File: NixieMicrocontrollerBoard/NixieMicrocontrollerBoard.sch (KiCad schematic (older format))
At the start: 12 parts, among them IC1 ATMEGA328-P, P1 CONN_01X03, P2 GPS_Header, P3 SD_Header, P4 Nixie_Header, Y1 16MHz

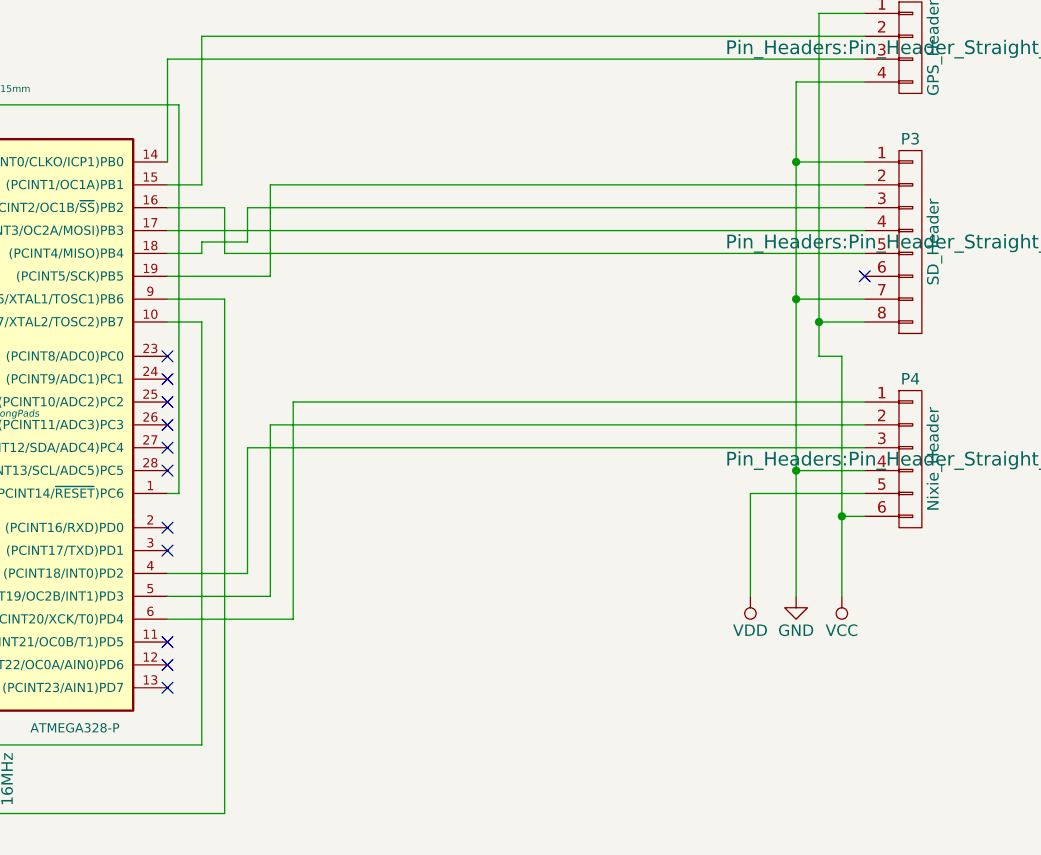
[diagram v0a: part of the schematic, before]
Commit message: Fixes up the microcontroller board, and adds a library to drive the Nixie boards
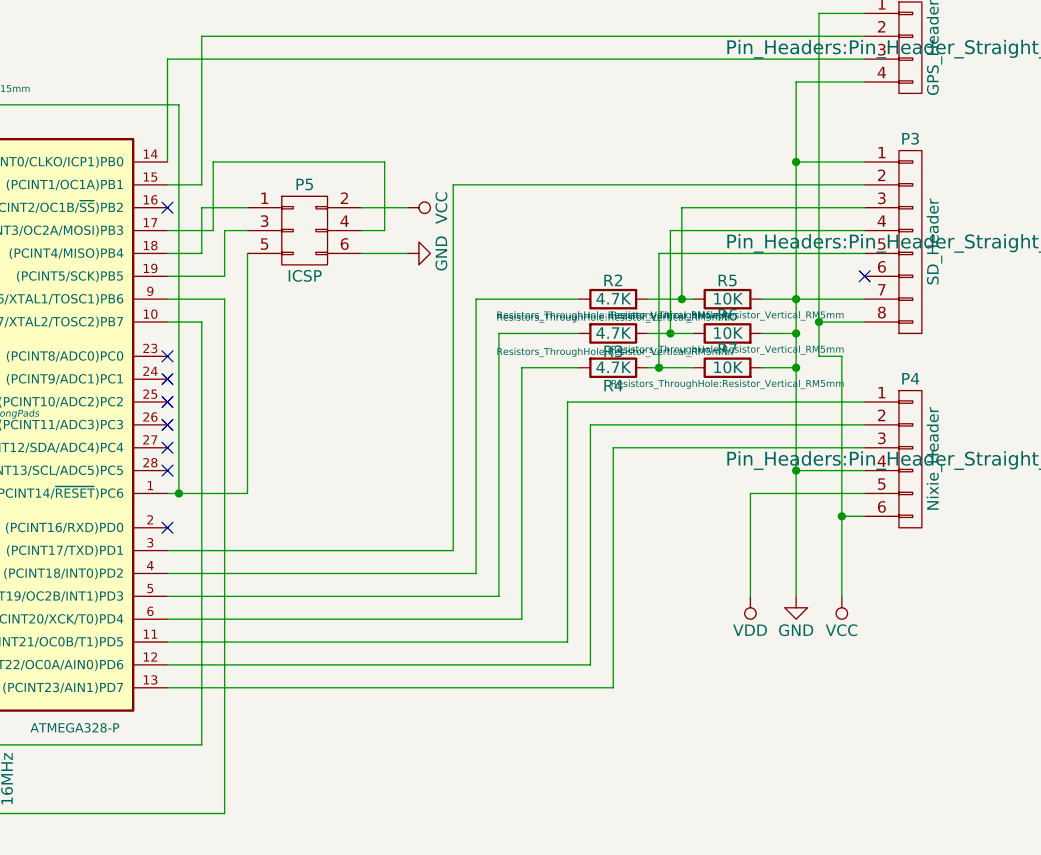
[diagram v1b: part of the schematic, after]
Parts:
- added P5: ICSP, Pin_Headers:Pin_Header_Straight_2x03, symbol CONN_02X03
- added R2, R3, R4: 4.7K, Resistors_ThroughHole:Resistor_Vertical_RM5mm, symbol R
- added R5, R6, R7: 10K, Resistors_ThroughHole:Resistor_Vertical_RM5mm, symbol R
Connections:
- net GND: now also P5.6 (P6), R5.2, R6.2, R7.2
- net VCC: now also P5.2 (P2)
- net at IC1.1 ((PCINT14/~RESET~)PC6), R1.1: now also P5.5 (P5)
- net at IC1.11 ((PCINT21/OC0B/T1)PD5): now also P4.1 (P1)
- net at IC1.12 ((PCINT22/OC0A/AIN0)PD6): now also P4.2 (P2)
- net at IC1.13 ((PCINT23/AIN1)PD7): now also P4.3 (P3)
- net at IC1.16 ((PCINT2/OC1B/~SS~)PB2): no longer P3.5 (P5)
- net at IC1.17 ((PCINT3/OC2A/MOSI)PB3): now also P5.4 (P4); no longer P3.4 (P4)
- net at IC1.18 ((PCINT4/MISO)PB4): now also P5.1 (P1); no longer P3.3 (P3)
- net at IC1.19 ((PCINT5/SCK)PB5): now also P5.3 (P3); no longer P3.2 (P2)
- net at IC1.3 ((PCINT17/TXD)PD1): now also P3.2 (P2)
- net at IC1.4 ((PCINT18/INT0)PD2): now also R2.1; no longer P4.3 (P3)
- net at IC1.5 ((PCINT19/OC2B/INT1)PD3): now also R3.2; no longer P4.2 (P2)
- net at IC1.6 ((PCINT20/XCK/T0)PD4): now also R4.2; no longer P4.1 (P1)
- new net: P3.3 (P3), R2.2, R5.1
- new net: P3.4 (P4), R3.1, R6.1
- new net: P3.5 (P5), R4.1, R7.1
- no-connect marks 12 -> 9

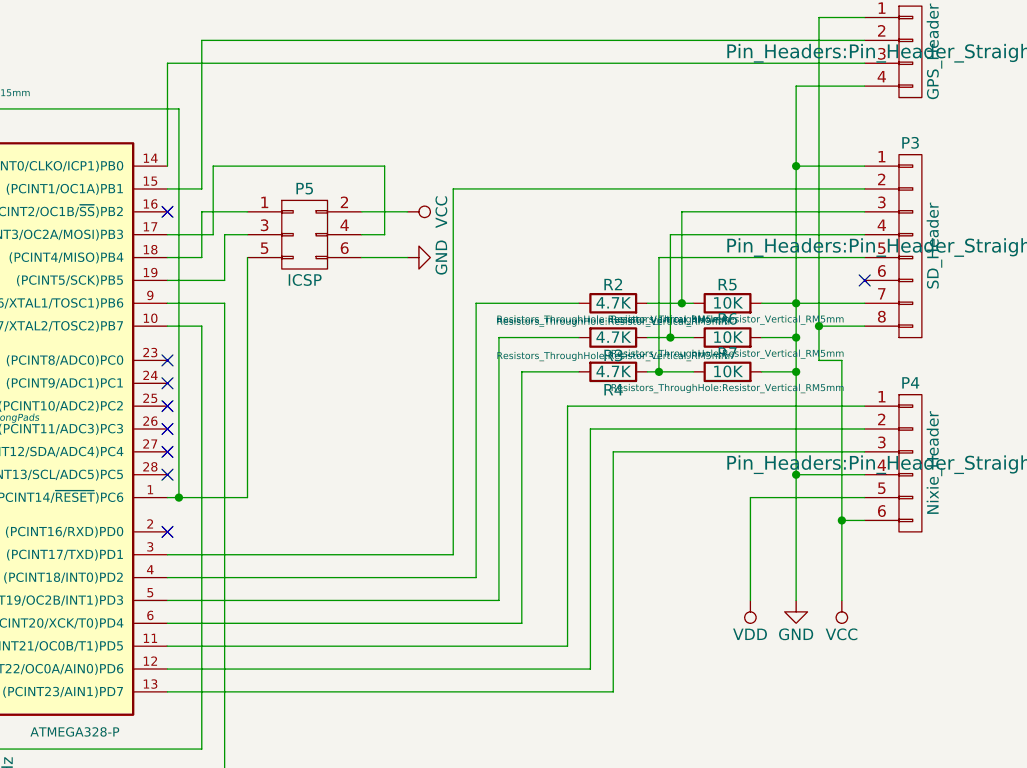
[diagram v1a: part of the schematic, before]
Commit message: Fixes the SD card pin connections to use the SPI bus
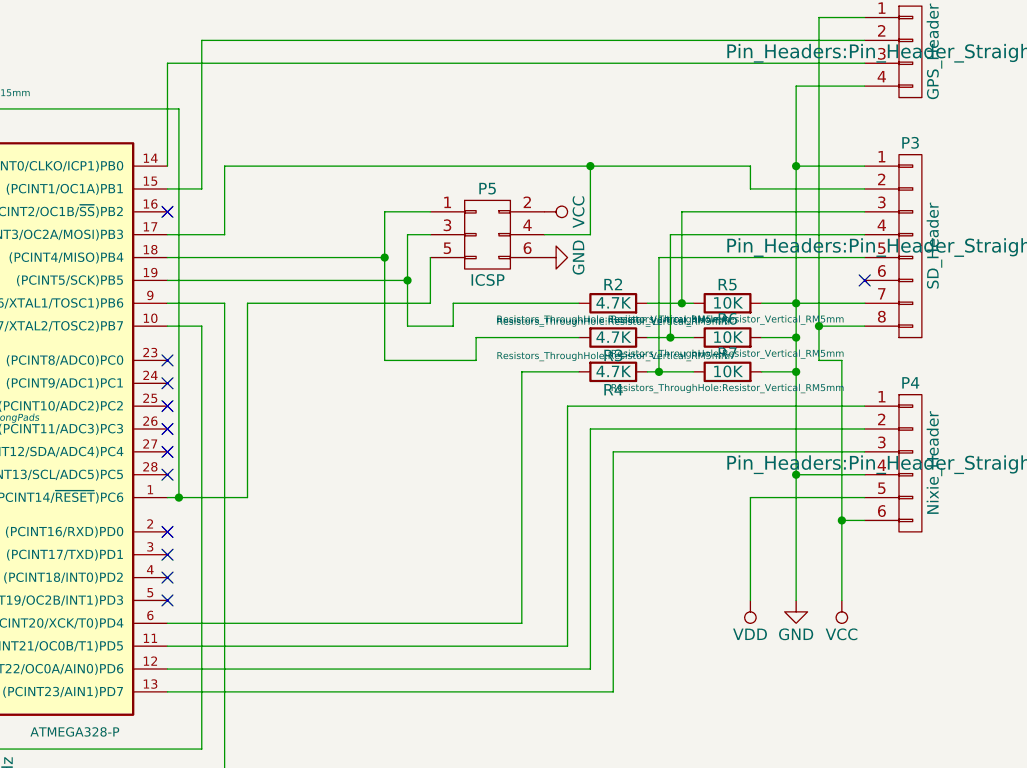
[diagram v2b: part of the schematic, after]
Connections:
- net at IC1.17 ((PCINT3/OC2A/MOSI)PB3), P5.4 (P4): now also P3.2 (P2)
- net at IC1.18 ((PCINT4/MISO)PB4), P5.1 (P1): now also R3.2
- net at IC1.19 ((PCINT5/SCK)PB5), P5.3 (P3): now also R2.1
- net at IC1.3 ((PCINT17/TXD)PD1): no longer P3.2 (P2)
- net at IC1.4 ((PCINT18/INT0)PD2): no longer R2.1
- net at IC1.5 ((PCINT19/OC2B/INT1)PD3): no longer R3.2
- no-connect marks 9 -> 12
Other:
- moved on the sheet: P5
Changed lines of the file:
@@
 	5900 2000 5750 2000
-Wire Wire Line
-	8800 2000 7000 2000
 Wire Wire Line
 	8800 3150 7700 3150
@@
 Connection ~ 7950 2650
 Wire Wire Line
-	7200 2650 7550 2650
-Wire Wire Line
 	8800 2300 7900 2300
 Wire Wire Line
@@
 	7300 2800 7300 3900
 Wire Wire Line
-	7100 2500 7550 2500
-Wire Wire Line
 	7500 2950 7500 4000
 Wire Wire Line
@@
 Wire Wire Line
 	7300 3900 5750 3900
-Wire Wire Line
-	7200 2650 7200 3800
-Wire Wire Line
-	7200 3800 5750 3800
-Wire Wire Line
-	7100 2500 7100 3700
-Wire Wire Line
-	7100 3700 5750 3700
-Wire Wire Line
-	7000 2000 7000 3600
-Wire Wire Line
-	7000 3600 5750 3600
 $Comp
 L CONN_02X03 P5
 U 1 1 5670CB51
-P 6350 2200
-F 0 "P5" H 6350 2400 50  0000 C CNN
-F 1 "ICSP" H 6350 2000 50  0000 C CNN
-F 2 "Pin_Headers:Pin_Header_Straight_2x03" H 6350 1000 60  0001 C CNN
-F 3 "" H 6350 1000 60  0000 C CNN
-	1    6350 2200
+P 7150 2200
+F 0 "P5" H 7150 2400 50  0000 C CNN
+F 1 "ICSP" H 7150 2000 50  0000 C CNN
+F 2 "Pin_Headers:Pin_Header_Straight_2x03" H 7150 1000 60  0001 C CNN
+F 3 "" H 7150 1000 60  0000 C CNN
+	1    7150 2200
 	1    0    0    -1
 $EndComp
 Wire Wire Line
-	6100 2100 5900 2100
-Wire Wire Line
-	5900 2100 5900 2300
-Wire Wire Line
-	5900 2300 5750 2300
-Wire Wire Line
-	6100 2200 6000 2200
-Wire Wire Line
-	6000 2200 6000 2400
-Wire Wire Line
-	6000 2400 5750 2400
-Wire Wire Line
-	6100 3350 6100 2300
+	6100 3350 6100 2500
 Connection ~ 5800 3350
 $Comp
 L VCC #PWR4
 U 1 1 5670CD95
-P 6800 2100
-F 0 "#PWR4" H 6800 1950 50  0001 C CNN
-F 1 "VCC" H 6800 2250 50  0000 C CNN
-F 2 "" H 6800 2100 60  0000 C CNN
-F 3 "" H 6800 2100 60  0000 C CNN
-	1    6800 2100
-	0    1    1    0
-$EndComp
-Wire Wire Line
-	6600 2200 6700 2200
-Wire Wire Line
-	6700 2200 6700 1900
-Wire Wire Line
-	6700 1900 5950 1900
-Wire Wire Line
-	5950 1900 5950 2200
-Wire Wire Line
-	5950 2200 5750 2200
+P 7400 2100
+F 0 "#PWR4" H 7400 1950 50  0001 C CNN
+F 1 "VCC" H 7400 2250 50  0000 C CNN
+F 2 "" H 7400 2100 60  0000 C CNN
+F 3 "" H 7400 2100 60  0000 C CNN
+	1    7400 2100
+	0    1    1    0
+$EndComp
+Wire Wire Line
+	7600 1900 7600 2200
+Wire Wire Line
+	6000 1900 8300 1900
+Wire Wire Line
+	6000 1900 6000 2200
+Wire Wire Line
+	6000 2200 5750 2200
 $Comp
 L GND #PWR5
 U 1 1 5670CE6C
-P 6800 2300
-F 0 "#PWR5" H 6800 2050 50  0001 C CNN
-F 1 "GND" H 6800 2150 50  0000 C CNN
-F 2 "" H 6800 2300 60  0000 C CNN
-F 3 "" H 6800 2300 60  0000 C CNN
-	1    6800 2300
-	0    -1   -1   0
-$EndComp
-Wire Wire Line
-	6600 2100 6800 2100
-Wire Wire Line
-	6800 2300 6600 2300
+P 7400 2300
+F 0 "#PWR5" H 7400 2050 50  0001 C CNN
+F 1 "GND" H 7400 2150 50  0000 C CNN
+F 2 "" H 7400 2300 60  0000 C CNN
+F 3 "" H 7400 2300 60  0000 C CNN
+	1    7400 2300
+	0    -1   -1   0
+$EndComp
+Wire Wire Line
+	7400 2100 7400 2100
+Wire Wire Line
+	7400 2300 7400 2300
 NoConn ~ 5750 3500
 NoConn ~ 5750 2100
+Wire Wire Line
+	8300 1900 8300 2000
+Wire Wire Line
+	8300 2000 8800 2000
+Connection ~ 7600 1900
+Wire Wire Line
+	6800 2400 5750 2400
+Wire Wire Line
+	6700 2300 5750 2300
+Wire Wire Line
+	6100 2500 6900 2500
+Wire Wire Line
+	7600 2200 7400 2200
+Wire Wire Line
+	6900 2500 6900 2300
+Wire Wire Line
+	6800 2200 6800 2600
+Wire Wire Line
+	6800 2200 6900 2200
+Wire Wire Line
+	6700 2100 6700 2750
+Wire Wire Line
+	6700 2100 6900 2100
+Wire Wire Line
+	6800 2600 7000 2600
+Wire Wire Line
+	7000 2600 7000 2500
+Wire Wire Line
+	7000 2500 7550 2500
+Connection ~ 6800 2400
+Wire Wire Line
+	7550 2650 7100 2650
+Wire Wire Line
+	7100 2650 7100 2750
+Wire Wire Line
+	7100 2750 6700 2750
+Connection ~ 6700 2300
+NoConn ~ 5750 3600
+NoConn ~ 5750 3700
+NoConn ~ 5750 3800
 $EndSCHEMATC

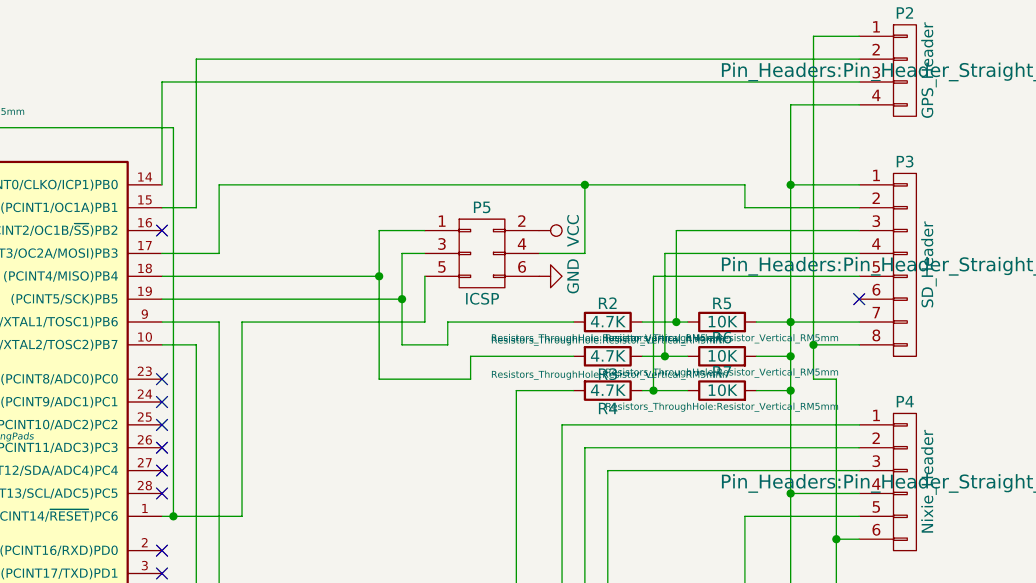
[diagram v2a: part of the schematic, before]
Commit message: Gets the sd card stuff mostly working
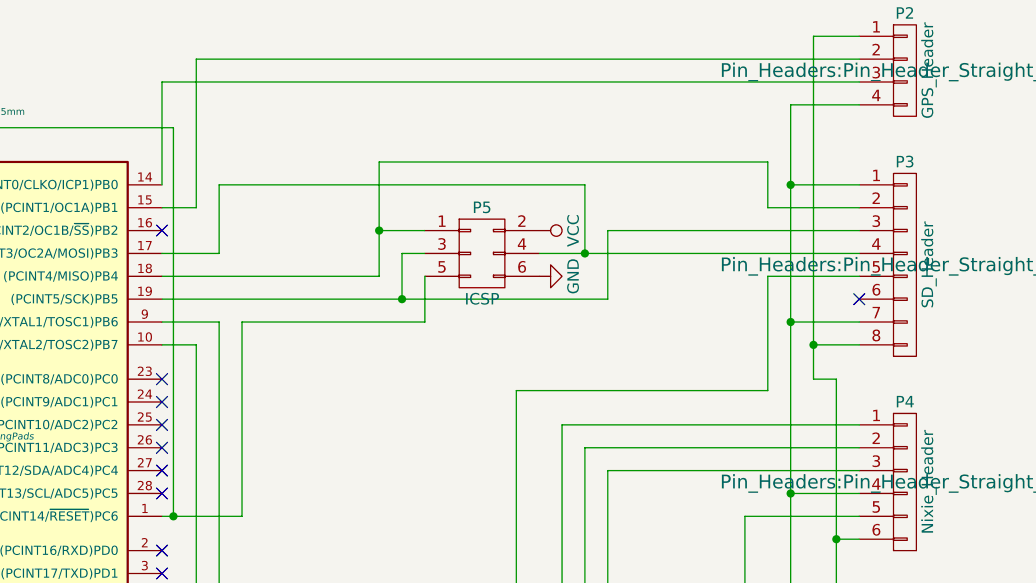
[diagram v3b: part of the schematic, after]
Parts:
- removed R2, R3, R4: 4.7K, Resistors_ThroughHole:Resistor_Vertical_RM5mm, symbol R
- removed R5, R6, R7: 10K, Resistors_ThroughHole:Resistor_Vertical_RM5mm, symbol R
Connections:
- net at IC1.17 ((PCINT3/OC2A/MOSI)PB3), P5.4 (P4): now also P3.4 (P4); no longer P3.2 (P2)
- net at IC1.18 ((PCINT4/MISO)PB4), P5.1 (P1): now also P3.2 (P2)
- net at IC1.19 ((PCINT5/SCK)PB5), P5.3 (P3): now also P3.3 (P3)
- net at IC1.6 ((PCINT20/XCK/T0)PD4): now also P3.5 (P5)
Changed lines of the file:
@@
 Connection ~ 8600 2600
 Wire Wire Line
-	8350 2500 8800 2500
+	8500 2500 8800 2500
 Connection ~ 8500 2500
 Wire Wire Line
@@
 	8600 2750 8700 2750
 Connection ~ 8700 3450
-$Comp
-L R R3
-U 1 1 566FC785
-P 7700 2650
-F 0 "R3" V 7780 2650 50  0000 C CNN
-F 1 "4.7K" V 7700 2650 50  0000 C CNN
-F 2 "Resistors_ThroughHole:Resistor_Vertical_RM5mm" V 7630 2650 30  0000 C CNN
-F 3 "" H 7700 2650 30  0000 C CNN
-	1    7700 2650
-	0    1    1    0
-$EndComp
-$Comp
-L R R2
-U 1 1 566FC809
-P 7700 2500
-F 0 "R2" V 7780 2500 50  0000 C CNN
-F 1 "4.7K" V 7700 2500 50  0000 C CNN
-F 2 "Resistors_ThroughHole:Resistor_Vertical_RM5mm" V 7630 2500 30  0000 C CNN
-F 3 "" H 7700 2500 30  0000 C CNN
-	1    7700 2500
-	0    -1   -1   0
-$EndComp
-$Comp
-L R R4
-U 1 1 566FCA5C
-P 7700 2800
-F 0 "R4" V 7780 2800 50  0000 C CNN
-F 1 "4.7K" V 7700 2800 50  0000 C CNN
-F 2 "Resistors_ThroughHole:Resistor_Vertical_RM5mm" V 7630 2800 30  0000 C CNN
-F 3 "" H 7700 2800 30  0000 C CNN
-	1    7700 2800
-	0    1    1    0
-$EndComp
-$Comp
-L R R5
-U 1 1 566FCA9A
-P 8200 2500
-F 0 "R5" V 8280 2500 50  0000 C CNN
-F 1 "10K" V 8200 2500 50  0000 C CNN
-F 2 "Resistors_ThroughHole:Resistor_Vertical_RM5mm" V 8130 2500 30  0000 C CNN
-F 3 "" H 8200 2500 30  0000 C CNN
-	1    8200 2500
-	0    -1   -1   0
-$EndComp
-$Comp
-L R R6
-U 1 1 566FCAEF
-P 8200 2650
-F 0 "R6" V 8280 2650 50  0000 C CNN
-F 1 "10K" V 8200 2650 50  0000 C CNN
-F 2 "Resistors_ThroughHole:Resistor_Vertical_RM5mm" V 8130 2650 30  0000 C CNN
-F 3 "" H 8200 2650 30  0000 C CNN
-	1    8200 2650
-	0    -1   -1   0
-$EndComp
-$Comp
-L R R7
-U 1 1 566FCB44
-P 8200 2800
-F 0 "R7" V 8280 2800 50  0000 C CNN
-F 1 "10K" V 8200 2800 50  0000 C CNN
-F 2 "Resistors_ThroughHole:Resistor_Vertical_RM5mm" V 8130 2800 30  0000 C CNN
-F 3 "" H 8200 2800 30  0000 C CNN
-	1    8200 2800
-	0    -1   -1   0
-$EndComp
 Wire Wire Line
-	8350 2650 8500 2650
-Connection ~ 8500 2650
-Wire Wire Line
-	8350 2800 8500 2800
-Connection ~ 8500 2800
-Wire Wire Line
-	7850 2500 8050 2500
-Wire Wire Line
-	8000 2100 8800 2100
-Wire Wire Line
-	8000 2100 8000 2500
-Connection ~ 8000 2500
-Wire Wire Line
-	7850 2650 8050 2650
-Wire Wire Line
-	7850 2800 8050 2800
-Wire Wire Line
-	8800 2200 7950 2200
-Wire Wire Line
-	7950 2200 7950 2650
-Connection ~ 7950 2650
-Wire Wire Line
-	8800 2300 7900 2300
-Wire Wire Line
-	7900 2300 7900 2800
-Connection ~ 7900 2800
-Wire Wire Line
-	7550 2800 7300 2800
+	7300 2800 8400 2800
 Wire Wire Line
 	7300 2800 7300 3900
@@
 	0    1    1    0
 $EndComp
-Wire Wire Line
-	7600 1900 7600 2200
-Wire Wire Line
-	6000 1900 8300 1900
-Wire Wire Line
-	6000 1900 6000 2200
-Wire Wire Line
-	6000 2200 5750 2200
 $Comp
 L GND #PWR5
@@
 NoConn ~ 5750 2100
 Wire Wire Line
-	8300 1900 8300 2000
-Wire Wire Line
-	8300 2000 8800 2000
-Connection ~ 7600 1900
-Wire Wire Line
-	6800 2400 5750 2400
+	5750 2400 7700 2400
 Wire Wire Line
 	6700 2300 5750 2300
 Wire Wire Line
-	6100 2500 6900 2500
-Wire Wire Line
-	7600 2200 7400 2200
+	7400 2200 8800 2200
 Wire Wire Line
 	6900 2500 6900 2300
 Wire Wire Line
-	6800 2200 6800 2600
-Wire Wire Line
 	6800 2200 6900 2200
 Wire Wire Line
-	6700 2100 6700 2750
-Wire Wire Line
 	6700 2100 6900 2100
-Wire Wire Line
-	6800 2600 7000 2600
-Wire Wire Line
-	7000 2600 7000 2500
-Wire Wire Line
-	7000 2500 7550 2500
-Connection ~ 6800 2400
-Wire Wire Line
-	7550 2650 7100 2650
-Wire Wire Line
-	7100 2650 7100 2750
-Wire Wire Line
-	7100 2750 6700 2750
-Connection ~ 6700 2300
 NoConn ~ 5750 3600
 NoConn ~ 5750 3700
 NoConn ~ 5750 3800
+Wire Wire Line
+	7600 2200 7600 1900
+Wire Wire Line
+	7600 1900 6000 1900
+Wire Wire Line
+	6000 1900 6000 2200
+Wire Wire Line
+	6000 2200 5750 2200
+Wire Wire Line
+	6700 1800 6700 2300
+Wire Wire Line
+	6800 2400 6800 2200
+Wire Wire Line
+	8800 2300 8400 2300
+Wire Wire Line
+	8400 2300 8400 2800
+Wire Wire Line
+	8800 2000 8400 2000
+Wire Wire Line
+	8400 2000 8400 1800
+Wire Wire Line
+	8400 1800 6700 1800
+Connection ~ 6700 2100
+Wire Wire Line
+	8800 2100 7700 2100
+Wire Wire Line
+	7700 2100 7700 2400
+Connection ~ 6800 2400
+Wire Wire Line
+	6100 2500 6900 2500
+Connection ~ 7600 2200
 $EndSCHEMATC
